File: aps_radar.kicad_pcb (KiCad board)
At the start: 2 copper layers, 304 parts, among them J1 TRIG_MUX_OUT, J10 RX3_RX4, J2 RX1_RX2, J3 POWER_IN, J4 Tx_Ant, J5 Rx1_Ant, J6 Rx2_Ant, J7 Rx3_Ant, J8 Rx4_Ant, J9 LMX2491_CONN, SW1 PA_EN, SW2 ON/OFF, U1 HMC717A, U10 HMC951A, U11 OPA227, U12 OPA227, U13 HMC717A, U14 HMC951A, U15 OPA227, U16 OPA227, U17 HMC540S, U18 ASDMB-100MHz, U19 OPA227, U2 HMC951A, U20 HMC431, U21 TQP5523, U22 LMX2491RTWR, U23 LP5900-TL3.3, U24 TPS82140, U25 TPS7A49, U26 LP5900-TL3.0, U27 TPS7A90, U28 TPS7A92, U3 OPA227, U4 OPA227, U5 HMC717A, U6 HMC951A, U7 OPA227, U8 OPA227, U9 HMC717A

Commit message: Layout updates
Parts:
- added H1: MountingHole, MountingHole:MountingHole_3.2mm_M3, F.Cu at (22.1, 185.2)
- added H2: MountingHole, MountingHole:MountingHole_3.2mm_M3, F.Cu at (22.1, 193.1)
- added H3: MountingHole, MountingHole:MountingHole_3.2mm_M3, F.Cu at (30.0, 185.2)
- added H4: MountingHole, MountingHole:MountingHole_3.2mm_M3, F.Cu at (30.0, 193.1)
- added R81: 50, Resistor_SMD:R_0402_1005Metric, F.Cu at (152.8, 26.5)
- added TL10: ic_taper, aps_radar_lib:IC_Taper_0.22_0.35, F.Cu at (150.4, 54.2)
- added TL11: ic_taper, aps_radar_lib:IC_Taper_0.22_0.35, F.Cu at (150.4, 49.0)
- added TL12: ic_taper, aps_radar_lib:IC_Taper_0.25_0.35, F.Cu at (138.6, 61.1)
- added TL13: ic_taper, aps_radar_lib:IC_Taper_0.25_0.35, F.Cu at (142.0, 64.1)
- added TL14: ic_taper, aps_radar_lib:IC_Taper_0.25_0.35, F.Cu at (150.4, 45.8)
- added TL15: ic_taper, aps_radar_lib:IC_Taper_0.25_0.35, F.Cu at (150.4, 40.0)
- added TL16: mitered_bend, aps_radar_lib:mitered_bend_50, F.Cu at (146.8, 63.9)
- added TL17: mitered_bend, aps_radar_lib:mitered_bend_50, F.Cu at (145.9, 47.1)
- added TL18: mitered_bend, aps_radar_lib:mitered_bend_50, F.Cu at (143.8, 46.7)
- added TL19: mitered_bend, aps_radar_lib:mitered_bend_50, F.Cu at (143.4, 38.6)
- added TL20: mitered_bend, aps_radar_lib:mitered_bend_50, F.Cu at (148.0, 58.1)
- added TL21: mitered_bend, aps_radar_lib:mitered_bend_50, F.Cu at (150.2, 57.7)
- added TL22: ic_taper, aps_radar_lib:IC_Taper_0.25_0.35, F.Cu at (138.6, 41.6)
- added TL6: mitered_bend, aps_radar_lib:mitered_bend_50, F.Cu at (156.8, 36.0)
- added TL7: mitered_bend, aps_radar_lib:mitered_bend_50, F.Cu at (157.2, 29.9)
- added TL8: mitered_bend, aps_radar_lib:mitered_bend_50, F.Cu at (156.8, 33.8)
- added TL9: mitered_bend, aps_radar_lib:mitered_bend_50, F.Cu at (157.2, 39.9)
- C100: footprint Capacitor_SMD:C_1206_3216Metric -> Capacitor_SMD:C_0603_1608Metric
- C76: footprint Capacitor_SMD:C_0805_2012Metric -> Capacitor_SMD:C_0603_1608Metric
- C84, C87, C89: footprint Capacitor_SMD:C_0603_1608Metric -> Capacitor_SMD:C_0402_1005Metric
- C90, C91, C92, C95, C96, C97: footprint Capacitor_SMD:C_0805_2012Metric -> Capacitor_SMD:C_0402_1005Metric
- R55, R56, R57: footprint Resistor_SMD:R_0603_1608Metric -> Resistor_SMD:R_0402_1005Metric
- TL1: value coupled_line_14dB -> coupled_line_14db
- U11, U12, U15, U16, U19, U3, U4, U7, U8: value OPA227 -> OPA192; footprint Package_SO:SOIC-8_3.9x4.9mm_P1.27mm -> Package_SO:VSSOP-8_3.0x3.0mm_P0.65mm
- U20: footprint aps_radar_lib:HMC-LP4 -> Package_DFN_QFN:QFN-24-1EP_4x4mm_P0.5mm_EP2.8x2.8mm
- moved SW2 181.5 mm to (-55.5, 40.8)
- moved U27 177.8 mm to (-34.6, 38.2)
- moved C106 173.8 mm to (-43.2, 19.3)
- moved C107 173.8 mm to (-43.2, 29.2)
- moved C109 173.8 mm to (-30.5, 19.3)
- moved U28 171.8 mm to (-24.9, 39.3)
- moved U24 168.5 mm to (-13.7, 29.6)
- moved U23 168.5 mm to (-28.6, 34.2)
- moved U26 166.1 mm to (-20.8, 34.5)
- moved J6 160.1 mm to (219.5, 106.9), turned to 180 degrees
- moved U13 156.5 mm to (201.9, 85.3)
- moved J3 154.4 mm to (-58.7, 29.5)
- moved U25 151.9 mm to (-4.28, 8.26)
- moved J8 146.2 mm to (219.5, 149.9), turned to 180 degrees
- moved J7 145.2 mm to (219.5, 128.4), turned to 180 degrees
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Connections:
- C77 pad 2: (no net) -> GND
- JP5 pad 1: (no net) -> GND
- R56 pad 2: (no net) -> GND
- R58 pad 1: (no net) -> GND
- TL1 pad 3: Net-(TL1-Pad3) -> Net-(R81-Pad1)
- TL1 pad 4: (no net) -> Net-(TL1-Pad4)
- TL2 pad 1: Net-(TL1-Pad3) -> Net-(TL1-Pad4)
- TL3 pad 1: Net-(TL2-Pad2) -> Net-(TL3-Pad1)
- TL4 pad 1: Net-(TL2-Pad3) -> Net-(TL4-Pad1)
- TL5 pad 1: Net-(TL5-Pad1) -> Net-(TL16-Pad1)
- TL5 pad 2: /transmitter/VCO_OUT -> Net-(TL17-Pad2)
- TL5 pad 3: /transmitter/LMX_FIN -> Net-(TL20-Pad1)
- U11 pad 1: Net-(U11-Pad1) -> (no net)
- U11 pad 8: Net-(U11-Pad1) -> (no net)
- U12 pad 1: Net-(U12-Pad1) -> (no net)
- U12 pad 8: Net-(U12-Pad1) -> (no net)
- U15 pad 1: Net-(U15-Pad1) -> (no net)
- U15 pad 8: Net-(U15-Pad1) -> (no net)
- U16 pad 1: Net-(U16-Pad1) -> (no net)
- U16 pad 8: Net-(U16-Pad1) -> (no net)
- U17 pad 11: Net-(C80-Pad1) -> Net-(TL11-Pad1)
- U17 pad 2: Net-(C74-Pad2) -> Net-(TL10-Pad1)
- U18 pad 2: (no net) -> GND
- U19 pad 1: Net-(U19-Pad1) -> (no net)
- U19 pad 8: Net-(U19-Pad1) -> (no net)
- U20 pad 16: Net-(TL5-Pad1) -> Net-(TL13-Pad1)
- U20 pad 22: Net-(C85-Pad1) -> Net-(TL12-Pad1)
- U21 pad 13: /transmitter/PA_OUT -> Net-(TL15-Pad1)
- U21 pad 3: /transmitter/ATTEN_OUT -> Net-(TL14-Pad1)
- U22 pad 24: /transmitter/LMX_CPOUT -> Net-(TL22-Pad1)
- U3 pad 1: Net-(U3-Pad1) -> (no net)
- U3 pad 8: Net-(U3-Pad1) -> (no net)
- U4 pad 1: Net-(U4-Pad1) -> (no net)
- U4 pad 8: Net-(U4-Pad1) -> (no net)
- U7 pad 1: Net-(U7-Pad1) -> (no net)
- U7 pad 8: Net-(U7-Pad1) -> (no net)
- U8 pad 1: Net-(U8-Pad1) -> (no net)
- U8 pad 8: Net-(U8-Pad1) -> (no net)
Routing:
- net VCC: track 0.00 -> 18.8 mm
- net Net-(TL17-Pad2): track 0.00 -> 11.5 mm
- net Net-(C78-Pad1): track 0.00 -> 8.12 mm
- net Net-(TL18-Pad2): track 0.00 -> 7.43 mm
- net /transmitter/LMX_CPOUT: track 0.00 -> 7.29 mm
- net Net-(R44-Pad1): track 0.00 -> 5.57 mm
- net /transmitter/PA_OUT: track 0.00 -> 4.56 mm
- net Net-(R60-Pad1): track 0.00 -> 3.93 mm
- net /transmitter/LMX_VCP: track 0.00 -> 3.90 mm
- net Net-(TL13-Pad2): track 0.00 -> 3.80 mm
- net Net-(TL7-Pad1): track 0.00 -> 3.27 mm
- net Net-(TL6-Pad2): track 0.00 -> 3.21 mm
- net Net-(C83-Pad1): track 0.00 -> 3.21 mm
- net Net-(C82-Pad1): track 0.00 -> 2.63 mm
- net Net-(C85-Pad1): track 0.00 -> 2.54 mm
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- added copper zone on F.Cu, net +3V3
- added copper zone on F.Cu, net Net-(C100-Pad1)
- added copper zone on F.Cu, net Net-(C75-Pad2)
- added copper zone on F.Cu, net Net-(C77-Pad1)
- added copper zone on F.Cu, net Net-(C81-Pad1)
- added copper zone on F.Cu, net Net-(C82-Pad1)
- added copper zone on F.Cu, net Net-(C86-Pad1)
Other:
- copper layers 2 -> 4
- net class 50-ohm added: clearance 0.32, trace_width 0.35, via_dia 0.508, via_drill 0.254
- net class 50-ohm-chip added: clearance 0.2, trace_width 0.35, via_dia 0.508, via_drill 0.254
- net class Default: via_dia 0.8 -> 0.508; via_drill 0.4 -> 0.254
- rule via_min_drill: 0.3 -> 0.254
- rule via_min_size: 0.4 -> 0.3

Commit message: Finished placing transmitter and power
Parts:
- removed C109: DNP, Capacitor_SMD:CP_Elec_8x11.9
- moved J10 278.3 mm to (203.1, 165.7), turned to 0 degrees
- moved J2 261.4 mm to (180.4, 165.5), turned to 0 degrees
- moved C23 189.4 mm to (181.0, 136.3)
- moved C24 189.4 mm to (177.2, 133.6)
- moved C4 189.4 mm to (206.7, 99.1)
- moved C49 189.4 mm to (262.9, 91.2)
- moved C50 189.4 mm to (253.3, 97.6)
- moved C52 189.4 mm to (262.9, 108.3)
- moved C53 189.4 mm to (253.3, 112.2)
- moved C7 189.4 mm to (206.7, 102.0)
- moved R20 189.4 mm to (262.9, 93.7)
- moved R21 189.4 mm to (257.3, 100.0)
- moved R22 189.4 mm to (253.3, 100.1)
- moved R23 189.4 mm to (257.3, 114.6)
- moved R24 189.4 mm to (253.3, 114.7)
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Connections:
- R46 pad 2: /LMX_TRIG2 -> Net-(J9-Pad10)
- U17 pad 9: Net-(U17-Pad9) -> (no net)
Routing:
- net /~ATTEN_4DB: track 1.12 -> 67.8 mm, vias 1 -> 2
- net /~ATTEN_1DB: track 0.98 -> 67.5 mm, vias 1 -> 2
- net /~ATTEN_2DB: track 1.01 -> 67.3 mm, vias 1 -> 2
- net /power/5V0_PGD: track 0.00 -> 62.9 mm, vias 0 -> 4
- net /~ATTEN_8DB: track 0.69 -> 61.5 mm, vias 1 -> 4
- net +3V3: track 0.00 -> 51.3 mm, vias 0 -> 2
- net /LMX_TRIG1: track 0.98 -> 37.4 mm, vias 1 -> 2
- net Net-(SW1-Pad2): track 0.00 -> 36.1 mm, vias 0 -> 1
- net /LMX_MUXOUT: track 0.00 -> 29.6 mm, vias 0 -> 2
- net /LMX_MOD: track 0.00 -> 22.0 mm, vias 0 -> 2
- net /transmitter/LMX_LE: track 0.00 -> 21.9 mm, vias 0 -> 2
- net /power/5V5_PGD: track 0.00 -> 18.7 mm, vias 0 -> 2
- net /transmitter/LMX_DATA: track 0.00 -> 15.6 mm, vias 0 -> 2
- net /LMX_TRIG2: track 1.82 -> 16.4 mm, vias 1 -> 2
- net /power/5V5_OUT: track 0.00 -> 13.2 mm, vias 0 -> 2
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- added copper zone on F.Cu, net +10V
- added copper zone on F.Cu, net +5V
- added copper zone on F.Cu, net +5V25
- added copper zone on F.Cu, net /+12V_IN
- added copper zone on F.Cu, net /power/5V5_OUT
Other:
- board outline added: 158.2 x 53 mm
- net class Power added: clearance 0.2, trace_width 0.45, via_dia 0.8, via_drill 0.4
- board text added: "+ -"
- board text added: "+12V"
- board text added: "Tx Attenuation"

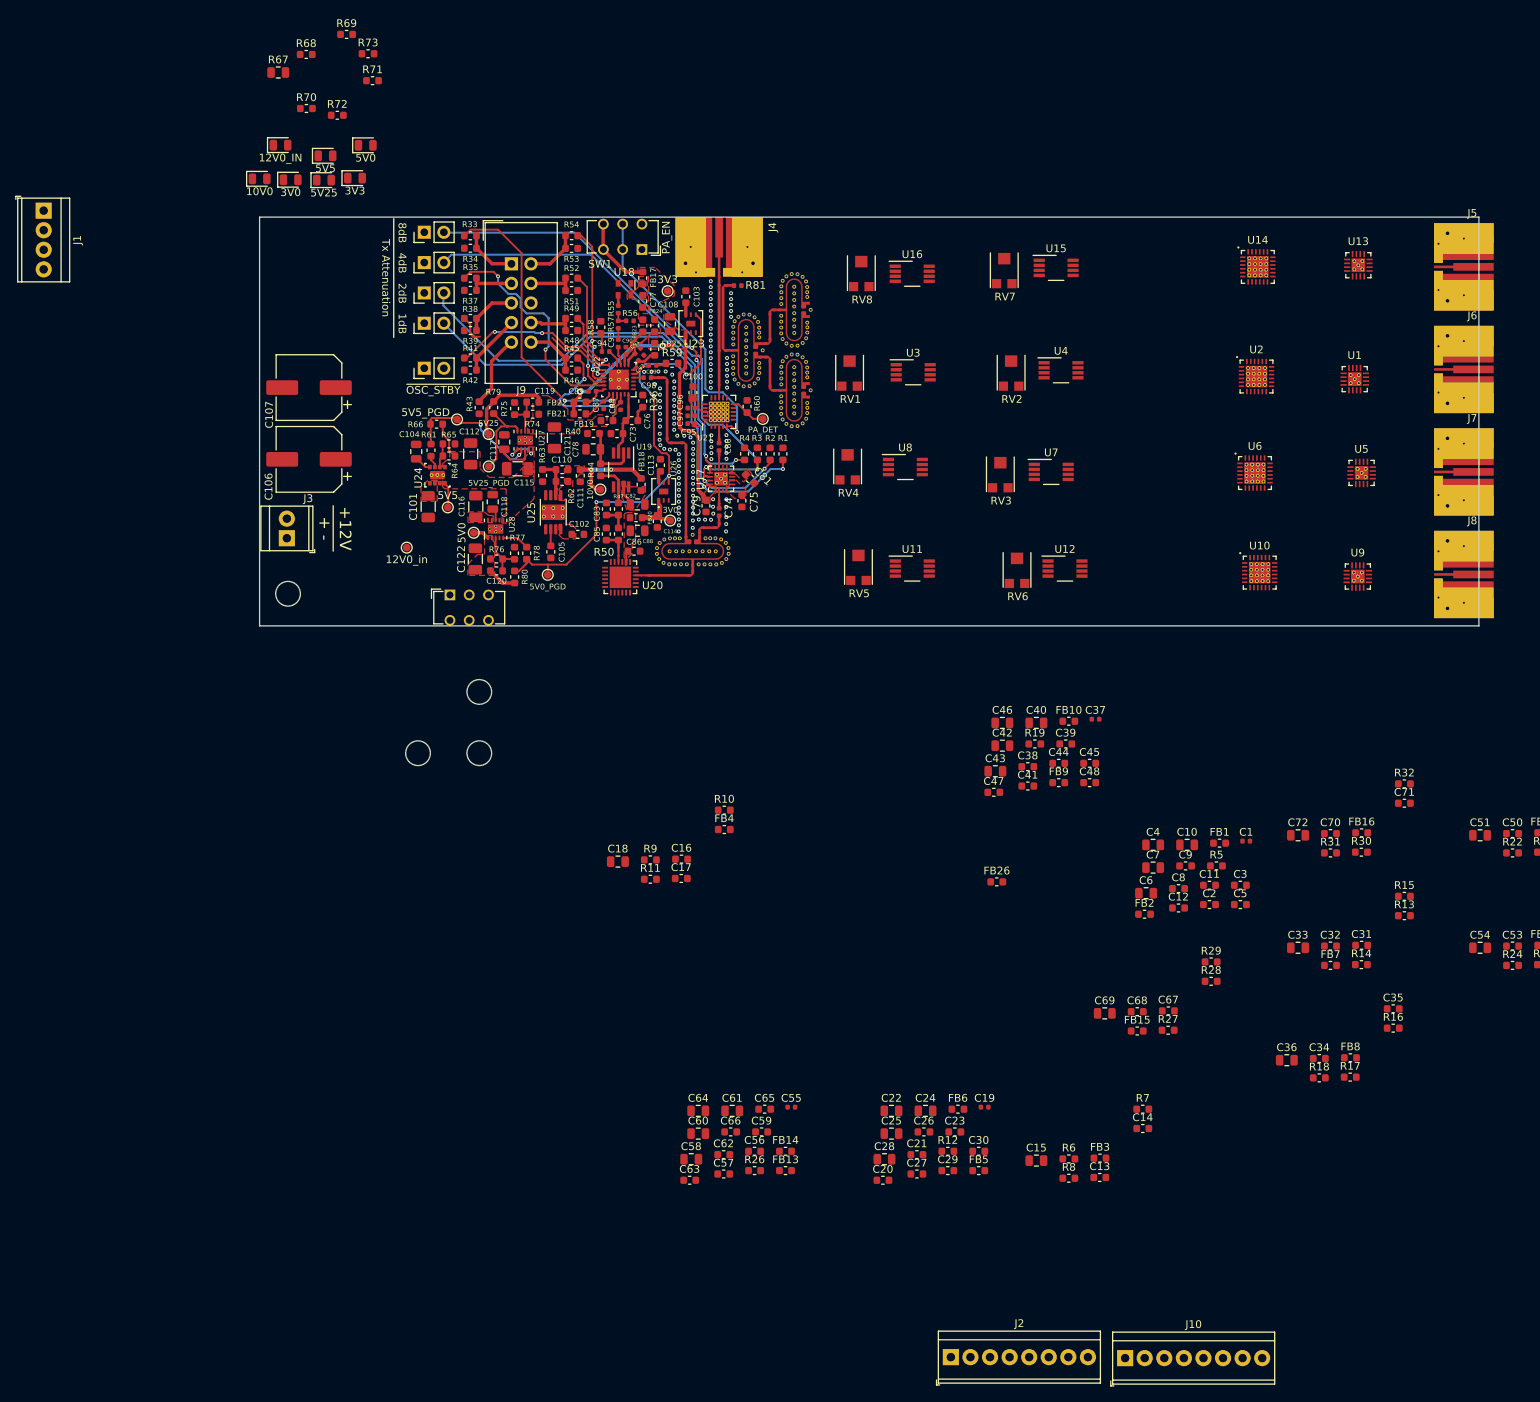
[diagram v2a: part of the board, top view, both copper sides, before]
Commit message: Began receiver layout
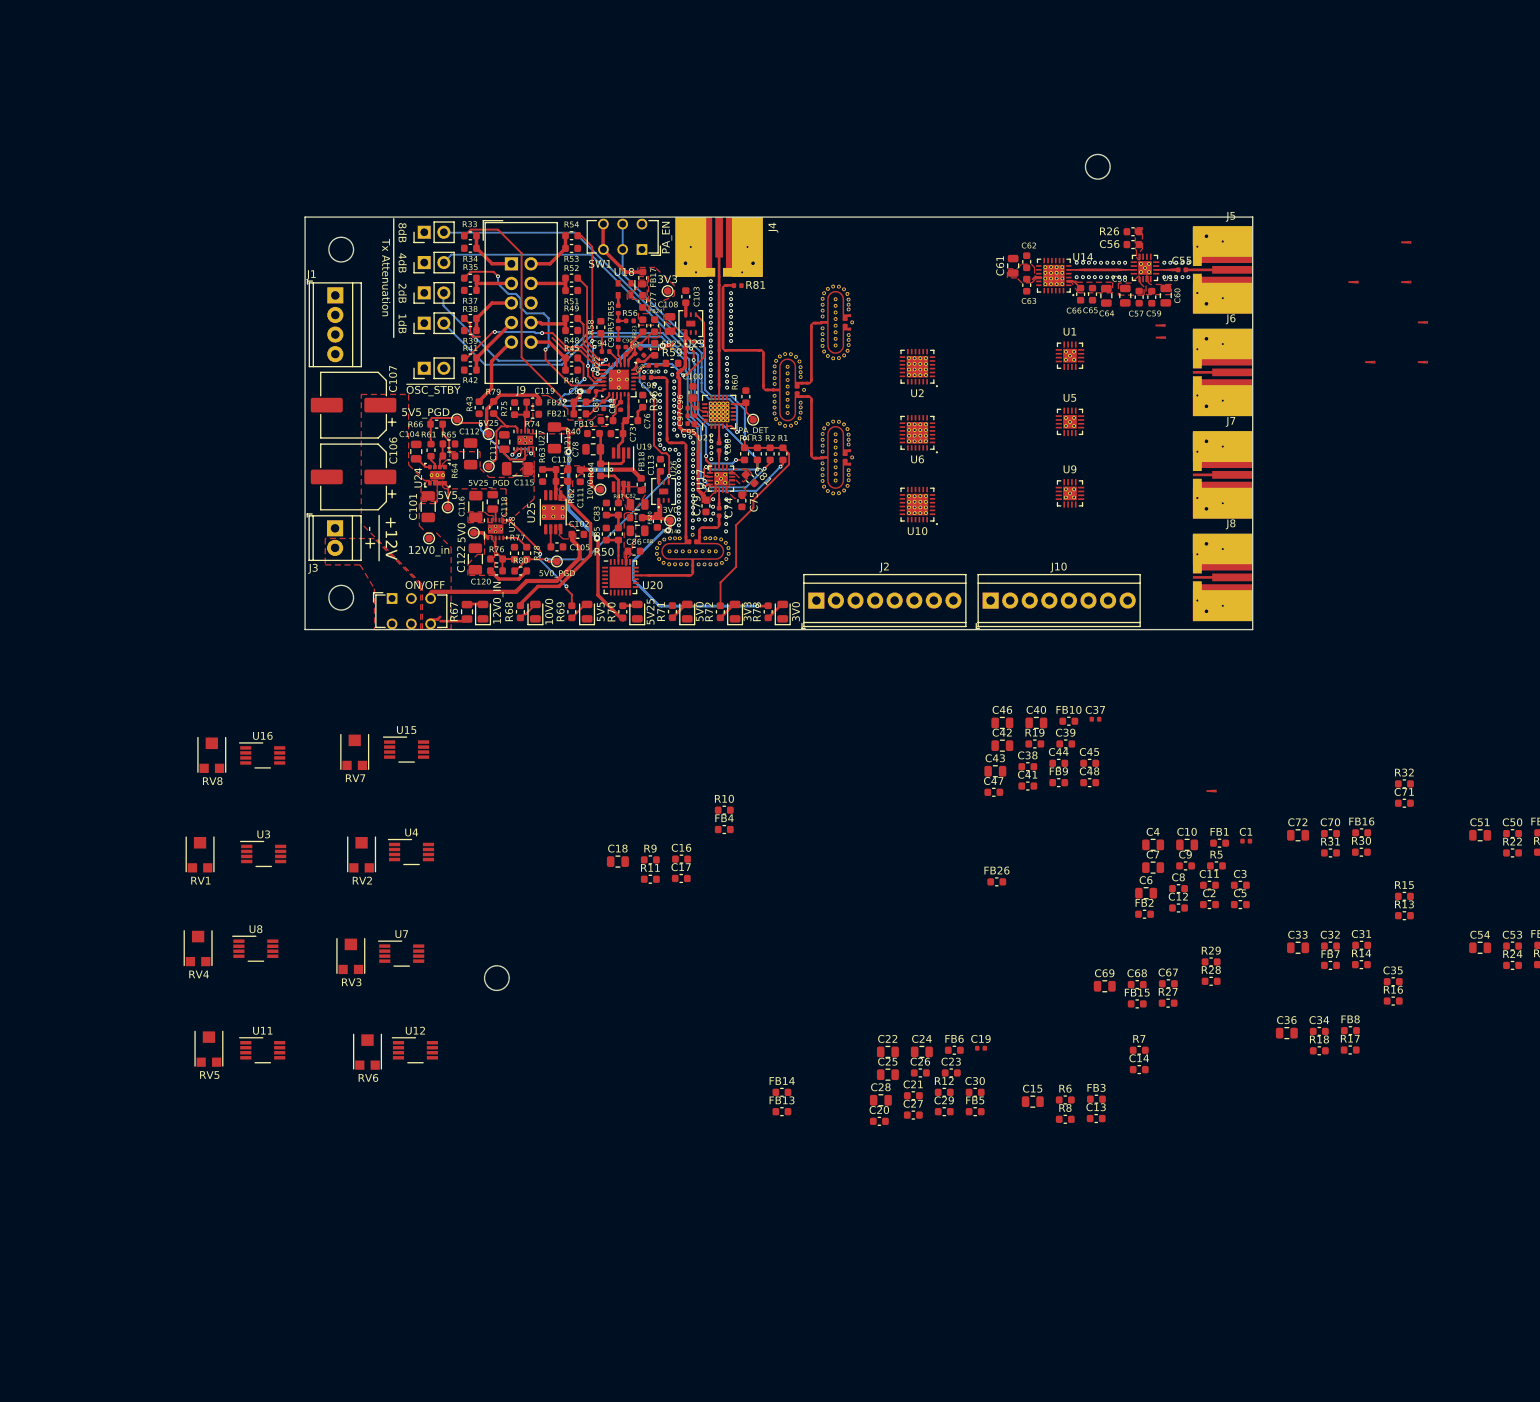
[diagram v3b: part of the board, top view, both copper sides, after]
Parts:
- added TL23: mitered_bend, aps_radar_lib:mitered_bend_50, F.Cu at (155.9, 35.1)
- added TL24: mitered_bend, aps_radar_lib:mitered_bend_50, F.Cu at (156.3, 39.9)
- added TL25: ic_taper, aps_radar_lib:IC_Taper_0.22_0.35, F.Cu at (214.2, 92.1)
- added TL26: ic_taper, aps_radar_lib:IC_Taper_0.22_0.35, F.Cu at (207.6, 33.3)
- added TL27: ic_taper, aps_radar_lib:IC_Taper_0.22_0.35, F.Cu at (207.6, 31.7)
- added TL28: ic_taper, aps_radar_lib:IC_Taper_0.22_0.35, F.Cu at (208.6, 24.5)
- added TL29: ic_taper, aps_radar_lib:IC_Taper_0.22_0.35, F.Cu at (232.6, 26.1)
- added TL30: ic_taper, aps_radar_lib:IC_Taper_0.22_0.35, F.Cu at (239.5, 20.9)
- added TL31: ic_taper, aps_radar_lib:IC_Taper_0.22_0.35, F.Cu at (239.5, 26.1)
- added TL32: ic_taper, aps_radar_lib:IC_Taper_0.22_0.35, F.Cu at (202.6, 24.5)
- added TL33: ic_taper, aps_radar_lib:IC_Taper_0.22_0.35, F.Cu at (234.8, 36.4)
- added TL34: ic_taper, aps_radar_lib:IC_Taper_0.22_0.35, F.Cu at (241.6, 31.3)
- added TL35: ic_taper, aps_radar_lib:IC_Taper_0.22_0.35, F.Cu at (241.6, 36.4)
- added TL36: ic_taper, aps_radar_lib:IC_Taper_0.22_0.35, F.Cu at (197.2, 24.5)
- moved R26 131.3 mm to (204.1, 19.5)
- moved C56 127.5 mm to (204.1, 21.2), turned to 180 degrees
- moved C57 125.9 mm to (204.9, 28.0), turned to 270 degrees
- moved C58 125.4 mm to (203.1, 27.8), turned to 270 degrees
- moved C60 124.5 mm to (208.3, 27.8), turned to 270 degrees
- moved C63 124.1 mm to (190.3, 26.5), turned to 90 degrees
- moved C62 122.3 mm to (190.3, 23.4), turned to 270 degrees
- moved C55 119.9 mm to (210.4, 24.5)
- moved C59 119.5 mm to (206.5, 28.0), turned to 270 degrees
- moved C64 118.3 mm to (200.6, 27.8), turned to 270 degrees
- moved C66 117.8 mm to (197.3, 27.6), turned to 90 degrees
- moved C61 115.5 mm to (188.5, 23.9), turned to 90 degrees
- moved C65 114.0 mm to (198.8, 27.6), turned to 90 degrees
- moved H4 110.6 mm to (199.5, 11.1)
- moved RV1 104.9 mm to (83.0, 100.2)
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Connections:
- C101 pad 1: /+12V_IN -> /power/+12V0_IN
- C102 pad 1: /+12V_IN -> /power/+12V0_IN
- C106 pad 1: /+12V_IN -> /power/+12V0_IN
- C107 pad 1: /+12V_IN -> /power/+12V0_IN
- J3 pad 2: /+12V_IN -> /power/+12V0_IN_CONN
- R67 pad 2: /+12V_IN -> /power/+12V0_IN
- R68 pad 2: +10V -> (no net)
- SW2 pad 2: /+12V_IN -> /power/+12V0_IN_CONN
- SW2 pad 3: /+12V_IN -> /power/+12V0_IN
- SW2 pad 5: /+12V_IN -> /power/+12V0_IN_CONN
- SW2 pad 6: /+12V_IN -> /power/+12V0_IN
- TL2 pad 1: Net-(TL1-Pad4) -> Net-(TL2-Pad1)
- TP3 pad 1: /+12V_IN -> /power/+12V0_IN
- U1 pad 11: /receiver_2/LNA_OUT -> Net-(TL29-Pad1)
- U1 pad 2: Net-(C1-Pad1) -> Net-(TL25-Pad1)
- U10 pad 5: /receiver_4/LNA_OUT -> Net-(TL35-Pad1)
- U13 pad 11: /receiver_1/LNA_OUT -> Net-(TL32-Pad1)
- U13 pad 2: Net-(C55-Pad1) -> Net-(TL28-Pad1)
- U14 pad 5: /receiver_1/LNA_OUT -> Net-(TL36-Pad1)
- U2 pad 5: /receiver_2/LNA_OUT -> Net-(TL33-Pad1)
- U24 pad 1: /+12V_IN -> /power/+12V0_IN
- U24 pad 2: /+12V_IN -> /power/+12V0_IN
- U25 pad 5: /+12V_IN -> /power/+12V0_IN
- U25 pad 8: /+12V_IN -> /power/+12V0_IN
- U5 pad 11: /receiver_3/LNA_OUT -> Net-(TL30-Pad1)
- U5 pad 2: Net-(C19-Pad1) -> Net-(TL26-Pad1)
- U6 pad 5: /receiver_3/LNA_OUT -> Net-(TL34-Pad1)
- U9 pad 11: /receiver_4/LNA_OUT -> Net-(TL31-Pad1)
- U9 pad 2: Net-(C37-Pad1) -> Net-(TL27-Pad1)
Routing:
- net +3V3: track 51.3 -> 101.5 mm, vias 2 -> 4
- net /power/+12V0_IN: track 0.00 -> 29.7 mm
- net +5V25: track 11.5 -> 40.8 mm, vias 0 -> 2
- net +3V0: track 6.27 -> 35.2 mm, vias 0 -> 2
- net +10V: track 11.2 -> 32.3 mm
- net /power/5V5_OUT: track 13.2 -> 28.7 mm, vias 2 -> 4
- net /receiver_1/LNA_OUT: track 0.00 -> 4.15 mm
- net Net-(TL23-Pad2): track 0.00 -> 4.03 mm
- net Net-(TL6-Pad2): track 3.21 -> 6.91 mm
- net Net-(TL1-Pad4): track 0.88 -> 4.38 mm
- net /power/5V0_PGD: track 62.9 -> 59.4 mm
- net Net-(TL7-Pad1): track 3.27 -> 6.65 mm
- net Net-(D3-Pad2): track 0.00 -> 2.75 mm
- net Net-(C61-Pad1): track 0.00 -> 2.70 mm
- net Net-(D2-Pad2): track 0.00 -> 2.69 mm
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- added copper zone on F.Cu, net /power/+12V0_IN
- added copper zone on F.Cu, net /power/+12V0_IN_CONN
- added copper zone on F.Cu, net Net-(C56-Pad1)
- added copper zone on F.Cu, net Net-(C57-Pad1)
- added copper zone on F.Cu, net Net-(C61-Pad1)
- removed copper zone on F.Cu, net /+12V_IN
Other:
- board size 158.2 x 53 mm -> 122.9 x 53.5 mm
- board text added: "- +"
- board text removed: "+ -"
